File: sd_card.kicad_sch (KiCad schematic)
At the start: 8 parts, among them J4 Micro_SD_Card

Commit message: fixed ERC errors
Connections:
- net GND: now also J4.9 (SHIELD)
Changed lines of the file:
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@@
+	(wire
+		(pts
+			(xy 168.91 93.98) (xy 168.91 99.06)
+		)
+		(stroke
+			(width 0)
+			(type default)
+		)
+	)
 	(wire
 		(pts
@@
 		(pts
 			(xy 105.41 66.04) (xy 105.41 88.9)
+		)
+		(stroke
+			(width 0)
+			(type default)
+		)
+	)
+	(wire
+		(pts
+			(xy 166.37 93.98) (xy 168.91 93.98)
 		)
 		(stroke
@@
 					(unit 1)
 				)
+			)
+		)
+	)
+	(symbol
+		(lib_id "power:GND")
+		(at 168.91 99.06 0)
+		(unit 1)
+		(exclude_from_sim no)
+		(in_bom yes)
+		(on_board yes)
+		(dnp no)
+		(property "Reference" "#PWR027"
+			(at 168.91 105.41 0)
+			(effects
+				(font
+					(size 1.27 1.27)
+				)
+				(hide yes)
+			)
+		)
+		(property "Value" "GND"
+			(at 168.91 102.87 0)
+			(effects
+				(font
+					(size 1.27 1.27)
+				)
+			)
+		)
+		(property "Footprint" ""
+			(at 168.91 99.06 0)
+			(effects
+				(font
+					(size 1.27 1.27)
+				)
+				(hide yes)
+			)
+		)
+		(property "Datasheet" ""
+			(at 168.91 99.06 0)
+			(effects
+				(font
+					(size 1.27 1.27)
+				)
+				(hide yes)
+			)
+		)
+		(property "Description" "Power symbol creates a global label with name \"GND\" , ground"
+			(at 168.91 99.06 0)
+			(effects
+				(font
+					(size 1.27 1.27)
+				)
+				(hide yes)
+			)
+		)
+		(pin "1"
+		)
+		(instances
+			(project "mic_patch_v1"
+				(path "/5448a297-4261-40a5-8009-47199bfe22cb/800536da-ce80-4a29-90e4-a5031f507197"
+					(reference "#PWR027")
+					(unit 1)
+				)

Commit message: swapped MOSI and MISO pins on SD ESD
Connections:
- net SD CSN: now also CR1.6; no longer CR1.4
- net SD MOSI: now also CR1.4; no longer CR1.6
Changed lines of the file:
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@@
-	)
-	(junction
-		(at 96.52 76.2)
-		(diameter 0)
-		(color 0 0 0 0)
 	)
 	(junction
@@
 	)
 	(junction
-		(at 100.33 73.66)
-		(diameter 0)
-		(color 0 0 0 0)
-	)
-	(junction
 		(at 109.22 86.36)
 		(diameter 0)
@@
 	)
 	(junction
+		(at 96.52 73.66)
+		(diameter 0)
+		(color 0 0 0 0)
+	)
+	(junction
 		(at 105.41 60.96)
 		(diameter 0)
@@
 	)
 	(junction
+		(at 100.33 76.2)
+		(diameter 0)
+		(color 0 0 0 0)
+	)
+	(junction
 		(at 113.03 60.96)
 		(diameter 0)
@@
 	(wire
 		(pts
-			(xy 100.33 73.66) (xy 100.33 118.11)
+			(xy 96.52 73.66) (xy 96.52 102.87)
 		)
 		(stroke
@@
 	(wire
 		(pts
-			(xy 96.52 76.2) (xy 113.03 76.2)
-		)
-		(stroke
-			(width 0)
-			(type default)
-		)
-	)
-	(wire
-		(pts
-			(xy 96.52 76.2) (xy 96.52 102.87)
+			(xy 53.34 76.2) (xy 100.33 76.2)
 		)
 		(stroke
@@
 	(wire
 		(pts
-			(xy 100.33 73.66) (xy 116.84 73.66)
+			(xy 52.07 73.66) (xy 96.52 73.66)
 		)
 		(stroke
@@
 	(wire
 		(pts
-			(xy 53.34 76.2) (xy 96.52 76.2)
-		)
-		(stroke
-			(width 0)
-			(type default)
-		)
-	)
-	(wire
-		(pts
 			(xy 96.52 118.11) (xy 100.33 118.11)
 		)
@@
 	(wire
 		(pts
-			(xy 52.07 73.66) (xy 100.33 73.66)
+			(xy 96.52 73.66) (xy 116.84 73.66)
 		)
 		(stroke
@@
 		)
 		(stroke
+			(width 0)
+			(type default)
+		)
+	)
+	(wire
+		(pts
+			(xy 100.33 76.2) (xy 100.33 118.11)
+		)
+		(stroke
+			(width 0)
+			(type default)
+		)
+	)
+	(wire
+		(pts
+			(xy 100.33 76.2) (xy 113.03 76.2)
+		)
+		(stroke

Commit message: fixed all major DRC warnings and errors
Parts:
- J4: LCSC PNs (none) -> C410348
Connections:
- net GND: now also J4.10 (SHIELD)
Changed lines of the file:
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@@
+	)
+	(junction
+		(at 168.91 93.98)
+		(diameter 0)
+		(color 0 0 0 0)
 	)
 	(junction
@@
 	(wire
 		(pts
+			(xy 165.1 91.44) (xy 168.91 91.44)
+		)
+		(stroke
+			(width 0)
+			(type default)
+		)
+	)
+	(wire
+		(pts
 			(xy 168.91 93.98) (xy 168.91 99.06)
 		)
@@
 		(pts
 			(xy 53.34 86.36) (xy 58.42 86.36)
+		)
+		(stroke
+			(width 0)
+			(type default)
+		)
+	)
+	(wire
+		(pts
+			(xy 168.91 91.44) (xy 168.91 93.98)
 		)
 		(stroke
@@
 			)
 		)
+		(property "LCSC PNs" "C410348"
+			(at 146.05 78.74 0)
+			(effects
+				(font
+					(size 1.27 1.27)
+				)
+				(hide yes)
+			)
+		)
 		(pin "1"
 		)
@@
 		(pin "9"
 		)
+		(pin "10"
+		)
 		(instances

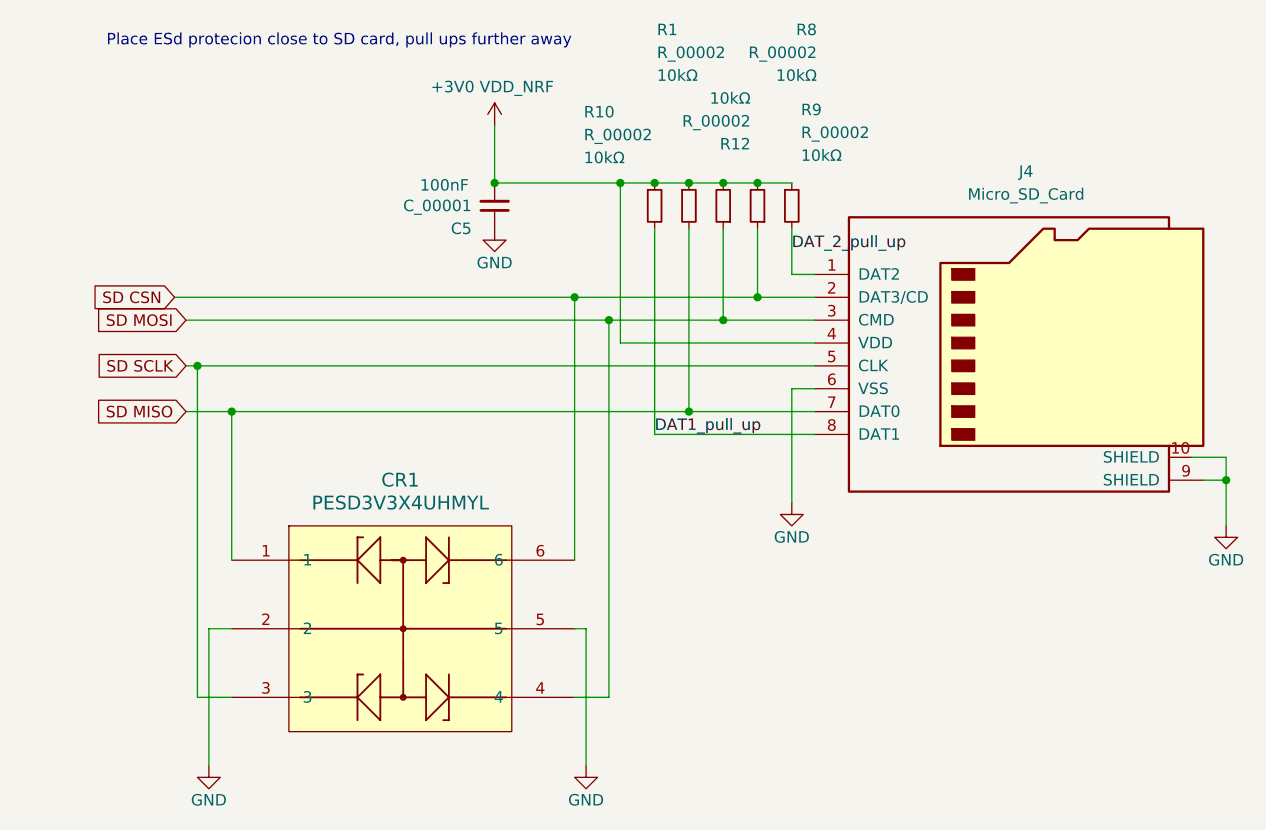
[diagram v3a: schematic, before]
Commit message: corrected missing part numbers + inconsistencies
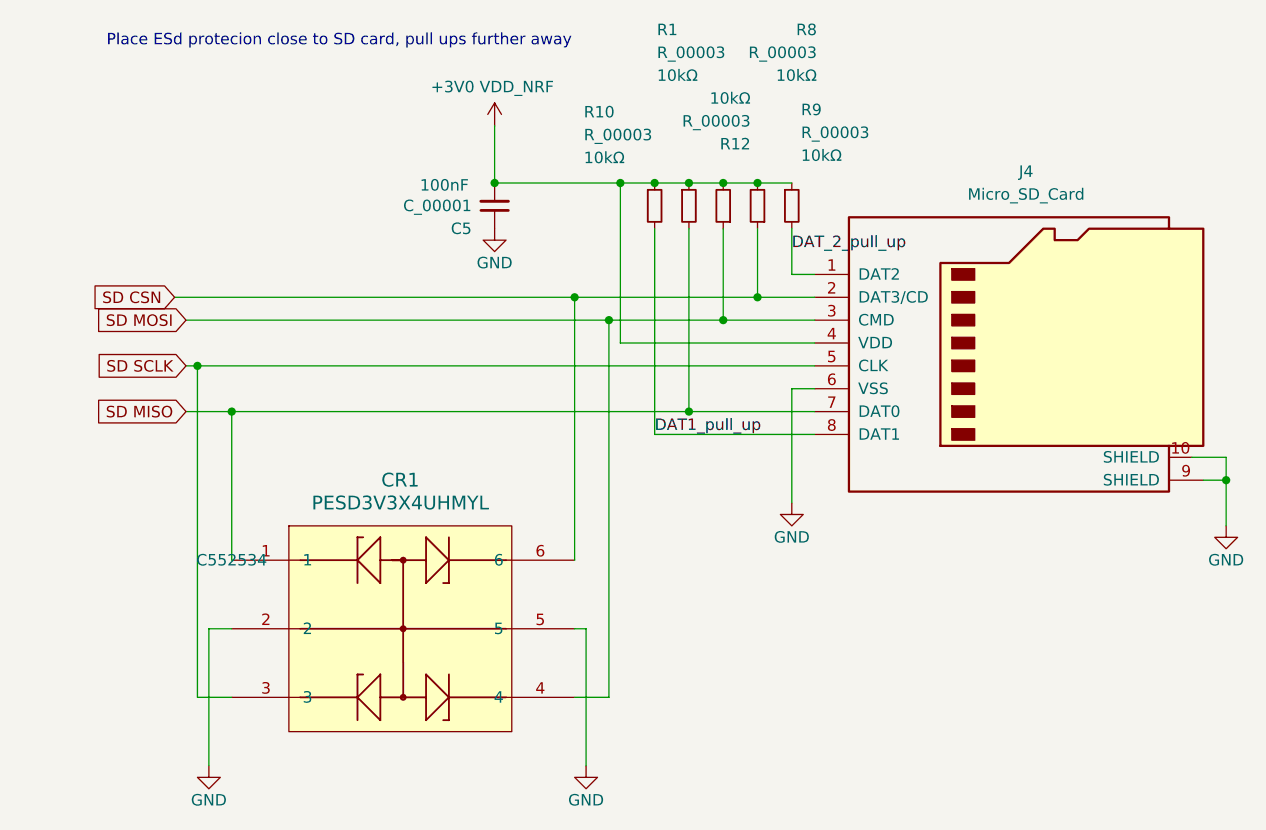
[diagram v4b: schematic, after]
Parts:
- CR1: LCSC PNs (none) -> C552534
- R1, R10, R12, R8, R9: value R_00002 -> R_00003
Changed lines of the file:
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@@
 			)
 		)
-		(property "Value" "R_00002"
+		(property "Value" "R_00003"
 			(at 105.664 46.482 0)
 			(effects
@@
 			)
 		)
-		(property "Value" "R_00002"
+		(property "Value" "R_00003"
 			(at 116.078 54.102 0)
 			(effects
@@
 			)
 		)
-		(property "Value" "R_00002"
+		(property "Value" "R_00003"
 			(at 97.536 55.626 0)
 			(effects
@@
 			)
 		)
+		(property "LC" ""
+			(at 58.42 102.87 0)
+			(effects
+				(font
+					(size 1.27 1.27)
+				)
+				(hide yes)
+			)
+		)
+		(property "LCSC PNs" "C552534"
+			(at 58.42 102.87 0)
+			(effects
+				(font
+					(size 1.27 1.27)
+				)
+			)
+		)
 		(pin "1"
 		)
@@
 			)
 		)
-		(property "Value" "R_00002"
+		(property "Value" "R_00003"
 			(at 123.444 46.482 0)
 			(effects
@@
 			)
 		)
-		(property "Value" "R_00002"
+		(property "Value" "R_00003"
 			(at 121.666 55.372 0)
 			(effects

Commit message: updated ESD footprint
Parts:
- CR1: footprint mic_patch_parts:DFN1308-6_SOT8006_NEX -> mic_patch_parts:SOT8006_C552534
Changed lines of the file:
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@@
 			)
 		)
-		(property "Footprint" "mic_patch_parts:DFN1308-6_SOT8006_NEX"
+		(property "Footprint" "mic_patch_parts:SOT8006_C552534"
 			(at 88.138 94.488 0)
 			(effects
